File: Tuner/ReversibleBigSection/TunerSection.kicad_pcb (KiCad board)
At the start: 2 copper layers, 100 x 100 mm, 112 parts, among them J1 Conn_01x03, J10 Conn_01x02, J11 Conn_02x05_Odd_Even, J12 Conn_01x01, J13 Conn_01x01, J14 Conn_01x01, J15 Conn_01x01, J2 Conn_01x03, J3 Conn_01x03, J4 Conn_01x03, J5 Conn_01x03, J6 Conn_01x03, J7 Conn_01x03, J8 Conn_01x02, J9 Conn_01x02, P10 Conn_01x01, P11 Conn_01x01, P12 Conn_01x01, P2 Conn_01x01, P3 Conn_01x01, P4 Conn_01x01, P5 Conn_01x01, P6 Conn_01x01, P7 Conn_01x01, P8 Conn_01x01, P9 Conn_01x01, U1 MCP23008, U2 ULN2803A

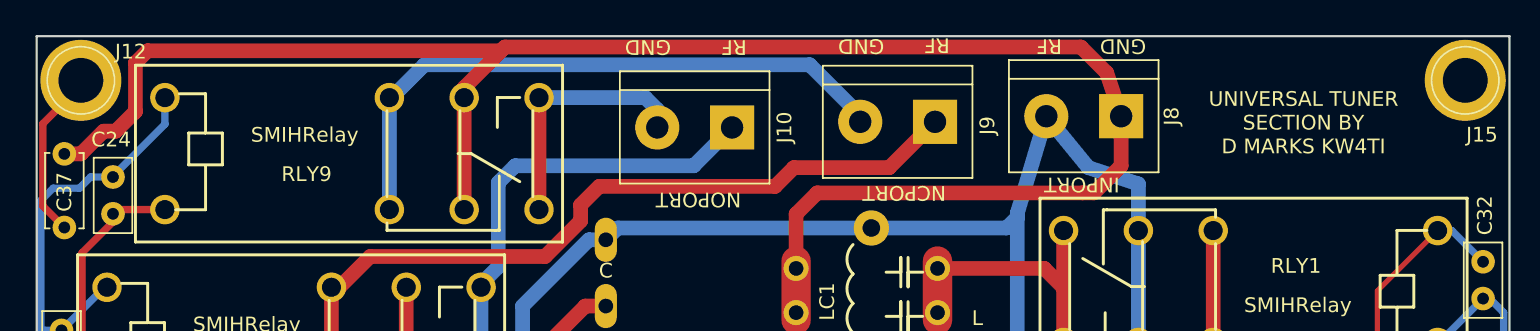
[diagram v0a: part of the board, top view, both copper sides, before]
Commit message: Added HK19F boards
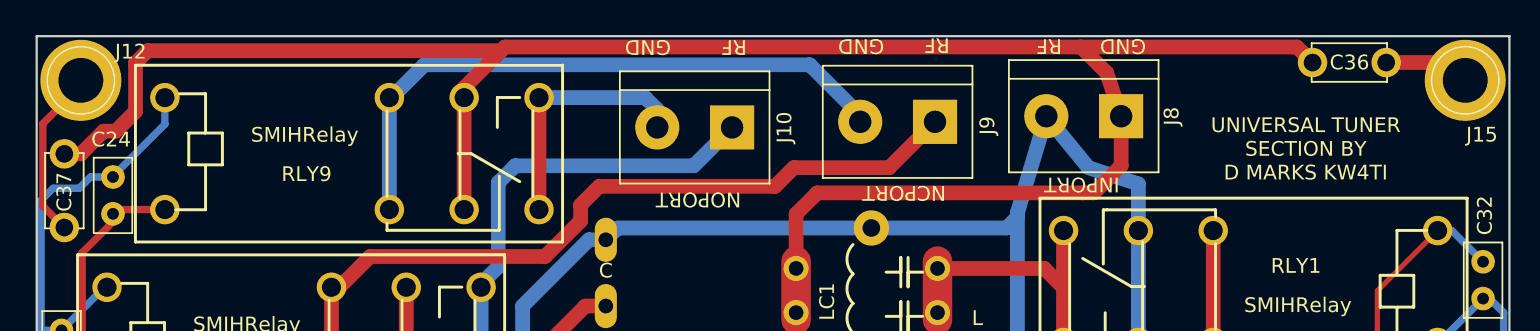
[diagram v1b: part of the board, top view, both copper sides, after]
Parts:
- added C36: 10 nF, Capacitors_THT:C_Disc_D5.0mm_W2.5mm_P5.00mm, F.Cu at (141.6, 51.8)
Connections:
- J15 pad 1: (no net) -> Net-(C36-Pad1)
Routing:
- net RFGND: track 185.3 -> 201.5 mm
- net Net-(C36-Pad1): track 0.00 -> 5.87 mm
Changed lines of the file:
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@@
 (kicad_pcb (version 4) (host pcbnew 4.0.7)
   (general
-    (links 280)
+    (links 282)
     (no_connects 0)
     (area 49.924999 49.924999 150.075001 150.075001)
     (thickness 1.6)
     (drawings 27)
-    (tracks 840)
+    (tracks 844)
     (zones 0)
-    (modules 112)
-    (nets 74)
+    (modules 113)
+    (nets 75)
   )
   (page A4)
@@
     (mod_text_size 1 1)
     (mod_text_width 0.15)
-    (pad_size 5.5 5.5)
-    (pad_drill 3.048)
+    (pad_size 2 2)
+    (pad_drill 1.2)
     (pad_to_mask_clearance 0.2)
     (aux_axis_origin 0 0)
@@
   (net 72 EXTPWR)
   (net 73 "Net-(C37-Pad1)")
+  (net 74 "Net-(C36-Pad1)")
   (net_class Default "This is the default net class."
     (clearance 0.2)
@@
     (add_net "Net-(C22-Pad1)")
     (add_net "Net-(C23-Pad2)")
+    (add_net "Net-(C36-Pad1)")
     (add_net "Net-(C37-Pad1)")
     (add_net "Net-(D1-Pad1)")
@@
     (fp_circle (center 0 0) (end 2.6 0) (layer F.CrtYd) (width 0.05))
     (fp_circle (center 0 0) (end 0 -2.286) (layer F.SilkS) (width 0.12))
-    (pad 1 thru_hole circle (at 0 0) (size 5.5 5.5) (drill 3.048) (layers *.Cu *.Mask))
+    (pad 1 thru_hole circle (at 0 0) (size 5.5 5.5) (drill 3.048) (layers *.Cu *.Mask)
+      (net 74 "Net-(C36-Pad1)"))
   )
   (module Capacitors_THT:C_Disc_D5.0mm_W2.5mm_P5.00mm (layer F.Cu)
@@
       (effects (font (size 1 1) (thickness 0.15)))
     )
-    (pad 1 thru_hole circle (at 0 0 90) (size 1.6 1.6) (drill 0.8) (layers *.Cu *.Mask)
+    (pad 1 thru_hole circle (at 0 0 90) (size 2 2) (drill 1.2) (layers *.Cu *.Mask)
       (net 73 "Net-(C37-Pad1)"))
-    (pad 2 thru_hole circle (at 5 0 90) (size 1.6 1.6) (drill 0.8) (layers *.Cu *.Mask)
+    (pad 2 thru_hole circle (at 5 0 90) (size 2 2) (drill 1.2) (layers *.Cu *.Mask)
       (net 1 RFGND))
     (model ${KISYS3DMOD}/Capacitors_THT.3dshapes/C_Disc_D5.0mm_W2.5mm_P5.00mm.wrl
@@
       (net 12 "Net-(J6-Pad2)"))
   )
+  (module Capacitors_THT:C_Disc_D5.0mm_W2.5mm_P5.00mm (layer F.Cu)
+    (at 141.6304 51.7906 180)
+    (descr "C, Disc series, Radial, pin pitch=5.00mm, , diameter*width=5*2.5mm^2, Capacitor, http://cdn-reichelt.de/documents/datenblatt/B300/DS_KERKO_TC.pdf")
+    (tags "C Disc series Radial pin pitch 5.00mm  diameter 5mm width 2.5mm Capacitor")
+    (fp_text reference C36 (at 2.4892 0 180) (layer F.SilkS)
+      (effects (font (size 1 1) (thickness 0.15)))
+    )
+    (fp_text value "10 nF" (at 2.5 2.56 180) (layer F.Fab)
+      (effects (font (size 1 1) (thickness 0.15)))
+    )
+    (fp_line (start 0 -1.25) (end 0 1.25) (layer F.Fab) (width 0.1))
+    (fp_line (start 0 1.25) (end 5 1.25) (layer F.Fab) (width 0.1))
+    (fp_line (start 5 1.25) (end 5 -1.25) (layer F.Fab) (width 0.1))
+    (fp_line (start 5 -1.25) (end 0 -1.25) (layer F.Fab) (width 0.1))
+    (fp_line (start -0.06 -1.31) (end 5.06 -1.31) (layer F.SilkS) (width 0.12))
+    (fp_line (start -0.06 1.31) (end 5.06 1.31) (layer F.SilkS) (width 0.12))
+    (fp_line (start -0.06 -1.31) (end -0.06 -0.996) (layer F.SilkS) (width 0.12))
+    (fp_line (start -0.06 0.996) (end -0.06 1.31) (layer F.SilkS) (width 0.12))
+    (fp_line (start 5.06 -1.31) (end 5.06 -0.996) (layer F.SilkS) (width 0.12))
+    (fp_line (start 5.06 0.996) (end 5.06 1.31) (layer F.SilkS) (width 0.12))
+    (fp_line (start -1.05 -1.6) (end -1.05 1.6) (layer F.CrtYd) (width 0.05))
+    (fp_line (start -1.05 1.6) (end 6.05 1.6) (layer F.CrtYd) (width 0.05))
+    (fp_line (start 6.05 1.6) (end 6.05 -1.6) (layer F.CrtYd) (width 0.05))
+    (fp_line (start 6.05 -1.6) (end -1.05 -1.6) (layer F.CrtYd) (width 0.05))
+    (fp_text user %R (at 2.5 0 180) (layer F.Fab)
+      (effects (font (size 1 1) (thickness 0.15)))
+    )
+    (pad 1 thru_hole circle (at 0 0 180) (size 2 2) (drill 1.2) (layers *.Cu *.Mask)
+      (net 74 "Net-(C36-Pad1)"))
+    (pad 2 thru_hole circle (at 5 0 180) (size 2 2) (drill 1.2) (layers *.Cu *.Mask)
+      (net 1 RFGND))
+    (model ${KISYS3DMOD}/Capacitors_THT.3dshapes/C_Disc_D5.0mm_W2.5mm_P5.00mm.wrl
+      (at (xyz 0 0 0))
+      (scale (xyz 1 1 1))
+      (rotate (xyz 0 0 0))
+    )
+  )
   (gr_text RF (at 97.3455 50.7365 180) (layer F.SilkS)
     (effects (font (size 1 1) (thickness 0.15)))
@@
   )
   (gr_line (start 150 50) (end 150 150) (angle 90) (layer Edge.Cuts) (width 0.15))
-  (gr_text "UNIVERSAL TUNER\nSECTION BY\nD MARKS KW4TI" (at 136.017 55.88) (layer F.SilkS)
+  (gr_text "UNIVERSAL TUNER\nSECTION BY\nD MARKS KW4TI" (at 136.1694 57.658) (layer F.SilkS)
     (effects (font (size 1 1) (thickness 0.15)))
   )
@@
   (segment (start 74.4616 110.0836) (end 74.772 110.394) (width 0.5) (layer B.Cu) (net 0))
   (segment (start 74.4616 110.0836) (end 74.772 110.394) (width 0.35) (layer B.Cu) (net 0))
+  (segment (start 120.904 50.7365) (end 135.5763 50.7365) (width 1) (layer F.Cu) (net 1))
+  (segment (start 135.5763 50.7365) (end 136.6304 51.7906) (width 1) (layer F.Cu) (net 1))
   (segment (start 121.031 60.6425) (end 121.793 60.6425) (width 1) (layer F.Cu) (net 1))
   (segment (start 123.6345 58.801) (end 123.6345 55.4355) (width 1) (layer F.Cu) (net 1) (status 20))
@@
   (segment (start 89.308 78.4495) (end 89.308 80.929) (width 1) (layer F.Cu) (net 22))
   (segment (start 80.1 79.8) (end 80.1 87.4) (width 1) (layer B.Cu) (net 22))
-  (segment (start 80.175 67.05) (end 80.175 66.8275) (width 1) (layer B.Cu) (net 23) (status C00000))
-  (segment (start 80.175 66.8275) (end 81.3435 65.659) (width 1) (layer B.Cu) (net 23) (status 400000))
-  (segment (start 94.615 58.801) (end 97.2185 56.1975) (width 1) (layer B.Cu) (net 23) (status 800000))
+  (segment (start 80.175 67.05) (end 80.175 66.8275) (width 1) (layer B.Cu) (net 23))
+  (segment (start 80.175 66.8275) (end 81.3435 65.659) (width 1) (layer B.Cu) (net 23))
+  (segment (start 94.615 58.801) (end 97.2185 56.1975) (width 1) (layer B.Cu) (net 23))
   (segment (start 82.4865 58.801) (end 94.615 58.801) (width 1) (layer B.Cu) (net 23))
   (segment (start 81.3435 59.944) (end 82.4865 58.801) (width 1) (layer B.Cu) (net 23))
@@
   (segment (start 76.327 51.943) (end 74.0945 54.1755) (width 1) (layer B.Cu) (net 39))
   (segment (start 74.0945 54.1755) (end 73.947 54.1755) (width 1) (layer B.Cu) (net 39))
-  (segment (start 84.107 54.1755) (end 84.107 61.7755) (width 1) (layer F.Cu) (net 40) (status C00000))
+  (segment (start 84.107 54.1755) (end 84.107 61.7755) (width 1) (layer F.Cu) (net 40))
   (segment (start 92.1385 56.1975) (end 92.1385 54.991) (width 1) (layer B.Cu) (net 40))
   (segment (start 92.1385 54.991) (end 91.323 54.1755) (width 1) (layer B.Cu) (net 40))
@@
   (segment (start 50.419 55.9435) (end 50.419 61.5315) (width 0.5) (layer F.Cu) (net 73))
   (segment (start 52.13604 53.86396) (end 53 53) (width 1) (layer F.Cu) (net 73) (status 30))
+  (segment (start 141.6304 51.7906) (end 145.7906 51.7906) (width 1) (layer F.Cu) (net 74))
+  (segment (start 145.7906 51.7906) (end 147 53) (width 1) (layer F.Cu) (net 74))
   (zone (net 25) (net_name GND) (layer F.Cu) (hatch edge 0.508)
     (connect_pads (clearance 0.5))

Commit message: JLCPCB Nov 1 2018
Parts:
- removed C36, C37: 10 nF, Capacitors_THT:C_Disc_D5.0mm_W2.5mm_P5.00mm
- added J16: Conn_01x01, tuner:SOLDERJUMPER, F.Cu at (74.5, 51.0)
- added J17: Conn_01x01, tuner:SOLDERJUMPER, F.Cu at (129.1, 52.9)
- added J18: Conn_01x01, tuner:SOLDERJUMPER, F.Cu at (141.8, 51.8)
- added J19: Conn_01x01, tuner:SOLDERJUMPER, F.Cu at (138.6, 51.8)
- added J20: Conn_01x01, tuner:SOLDERJUMPER, F.Cu at (60.0, 50.9)
- added J21: Conn_01x01, tuner:SOLDERJUMPER, F.Cu at (64.8, 50.9)
- added J22: Conn_01x01, tuner:SOLDERJUMPER, F.Cu at (88.5, 56.7)
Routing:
- net RFGND: track 201.5 -> 156.1 mm
- net Net-(J16-Pad1): track 42.4 -> 45.9 mm
- net Net-(J15-Pad1): track 5.87 -> 9.39 mm
- net Net-(J10-Pad2): track 17.2 -> 19.9 mm

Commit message: First code commit
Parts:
- moved RLY9 0.64 mm to (68.7, 57.3)
- moved RLY8 0.44 mm to (64.8, 70.4)
- moved RLY7 0.20 mm to (64.6, 83.4)
- moved RLY6 0.13 mm to (64.6, 96.5)
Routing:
- net RLYPWR: track 358.8 -> 359.8 mm

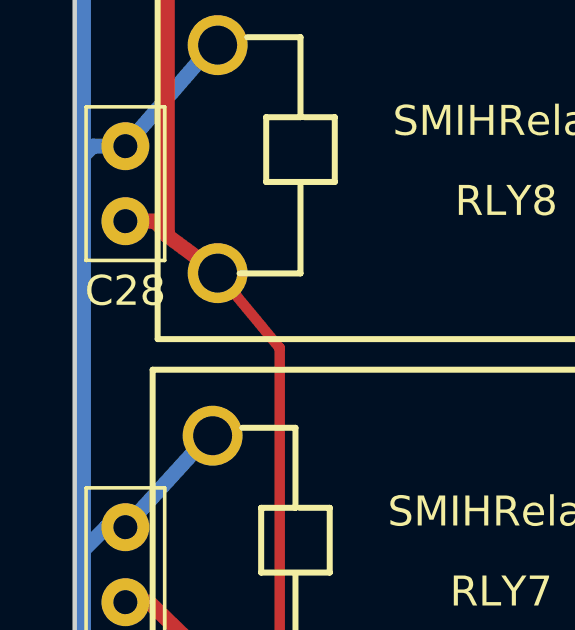
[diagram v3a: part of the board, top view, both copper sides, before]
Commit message: Removed 1k resistors, did some more rearranging on TandemMatch
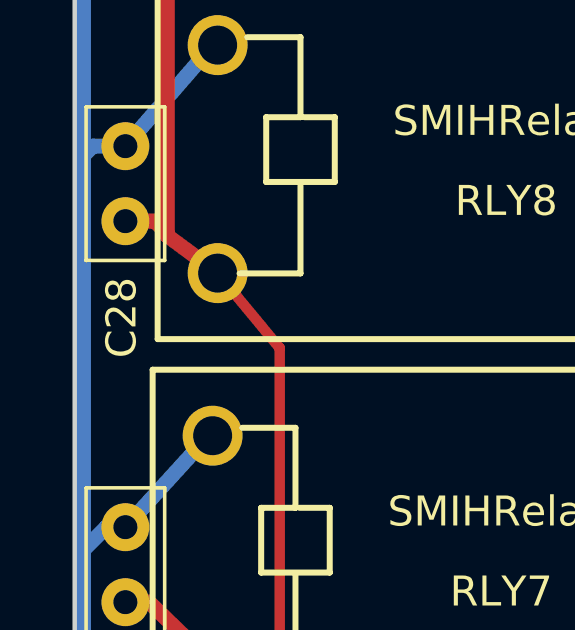
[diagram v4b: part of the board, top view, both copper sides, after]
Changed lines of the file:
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@@
     (links 285)
     (no_connects 0)
-    (area 44.281218 45.69208 151.844 153.921938)
+    (area 49.924999 49.924999 150.075001 150.075001)
     (thickness 1.6)
     (drawings 27)
@@
     (descr "C, Disc series, Radial, pin pitch=2.50mm, , diameter*width=5*2.5mm^2, Capacitor, http://cdn-reichelt.de/documents/datenblatt/B300/DS_KERKO_TC.pdf")
     (tags "C Disc series Radial pin pitch 2.50mm  diameter 5mm width 2.5mm Capacitor")
-    (fp_text reference C28 (at 4.826 0 360) (layer F.SilkS)
+    (fp_text reference C28 (at 5.715 0.127 450) (layer F.SilkS)
       (effects (font (size 1 1) (thickness 0.15)))
     )

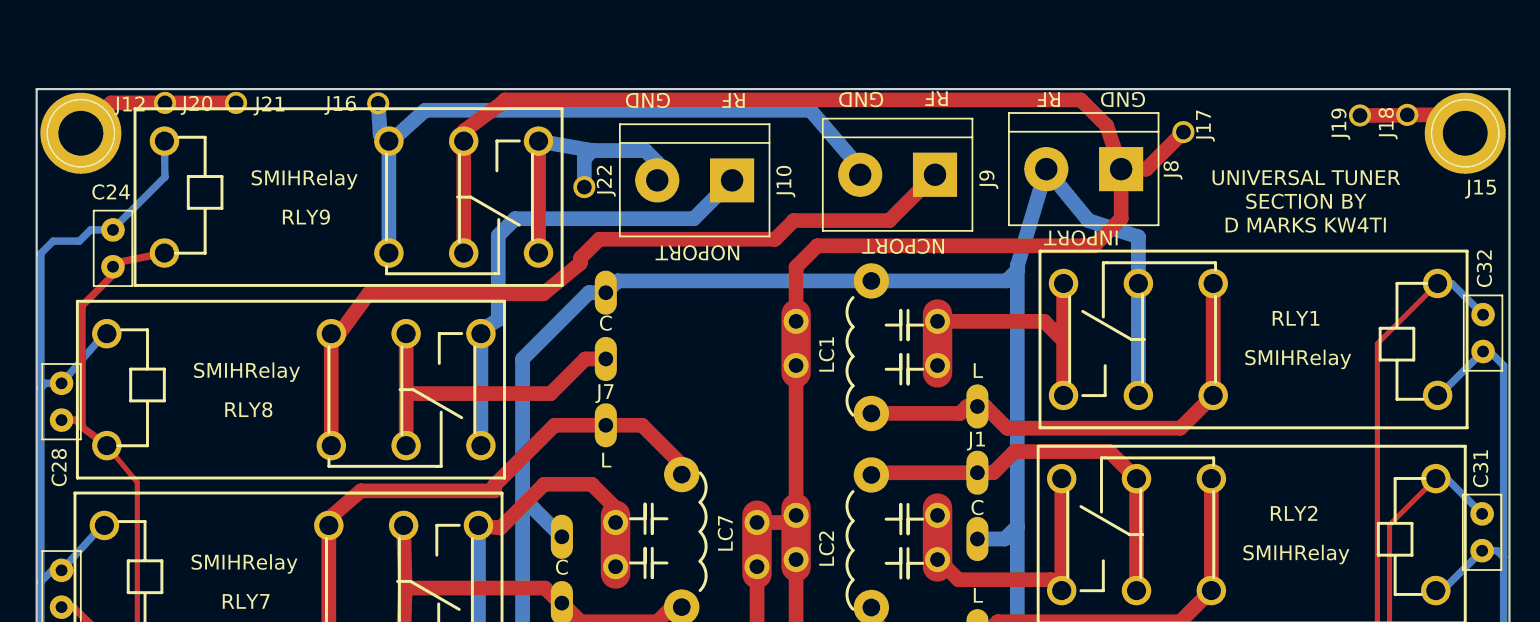
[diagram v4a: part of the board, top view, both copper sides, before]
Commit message: Modified connectors on Reversible boards
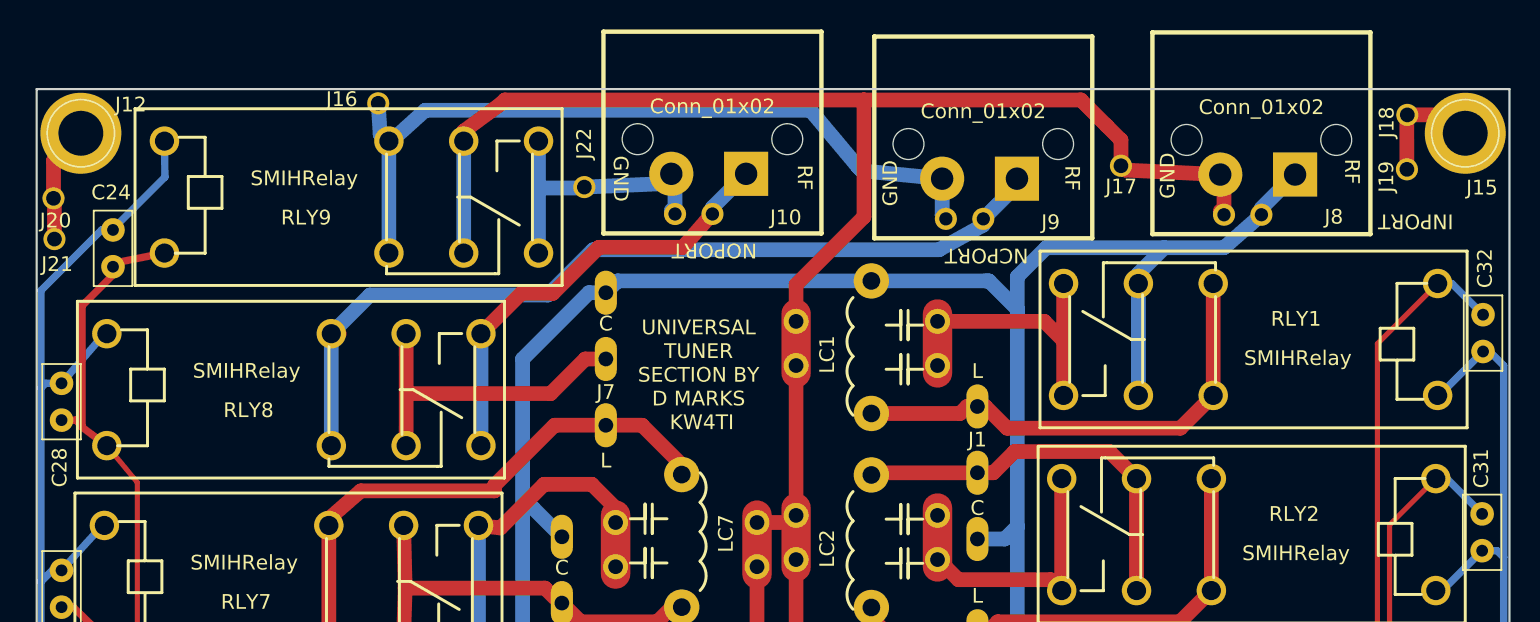
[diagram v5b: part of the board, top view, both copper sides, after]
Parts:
- J10, J8, J9: footprint Connectors_Terminal_Blocks:TerminalBlock_bornier-2_P5.08mm -> tuner:bnc_90_1-1337543-0_pad_combo
- moved J21 15.4 mm to (52.5, 60.2)
- moved J8 13.3 mm to (133.2, 46.2)
- moved J10 10.2 mm to (95.9, 46.1)
- moved J20 9.96 mm to (52.4, 57.4)
- moved J9 9.94 mm to (114.3, 46.4)
- moved J19 4.85 mm to (141.8, 55.4)
- moved J17 4.82 mm to (124.9, 55.2)
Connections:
- J8 pad 1: RFGND -> RFPORT1
- J8 pad 2: RFPORT1 -> RFGND
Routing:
- net RFGND: track 155.7 -> 147.0 mm
- net Net-(J16-Pad1): track 45.5 -> 53.6 mm
- net RFPORT1: track 161.1 -> 168.9 mm
- net Net-(J9-Pad1): track 53.4 -> 59.3 mm
- net Net-(J12-Pad1): track 13.0 -> 9.57 mm
- net Net-(J10-Pad1): track 32.3 -> 30.7 mm
- net RLYPWR: track 359.8 -> 358.3 mm

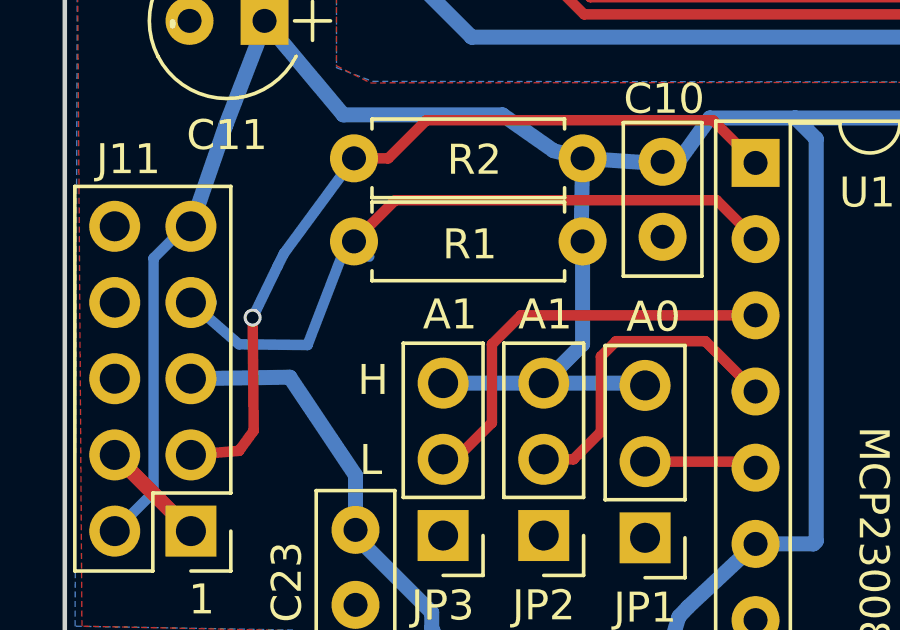
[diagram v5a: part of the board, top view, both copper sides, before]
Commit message: Symmetrized QuadCoupler Layout
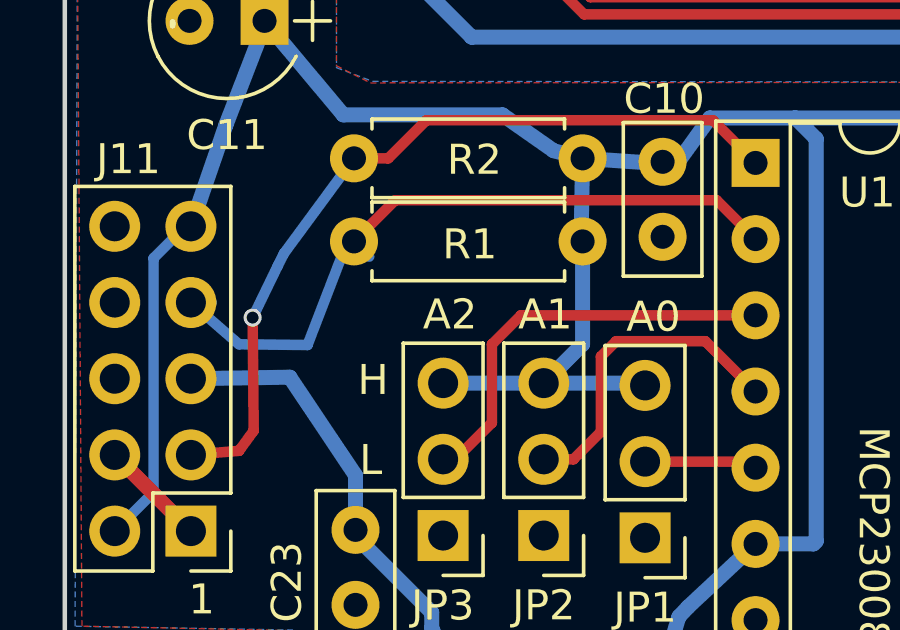
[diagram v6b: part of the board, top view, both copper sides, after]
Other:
- board text added: "A2"
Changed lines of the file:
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@@
     (links 291)
     (no_connects 0)
-    (area 49.924999 49.924999 150.075001 150.075001)
+    (area 44.281218 45.651 151.844 153.921938)
     (thickness 1.6)
     (drawings 27)
@@
   )
   (setup
-    (last_trace_width 1)
+    (last_trace_width 0.25)
     (user_trace_width 0.35)
     (user_trace_width 0.5)
@@
     (effects (font (size 1 1) (thickness 0.15)))
   )
-  (gr_text A1 (at 62.8396 132.8166) (layer F.SilkS)
+  (gr_text A2 (at 62.8396 132.8166) (layer F.SilkS)
     (effects (font (size 1 1) (thickness 0.15)))
   )

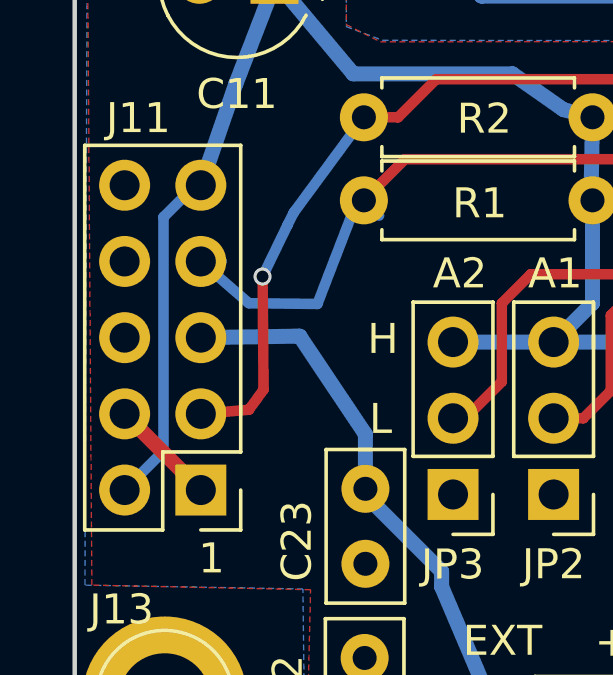
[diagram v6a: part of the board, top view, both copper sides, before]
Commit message: Changed I2C cable pinoutgit add Tunergit add Tuner Also added ICOM rig support
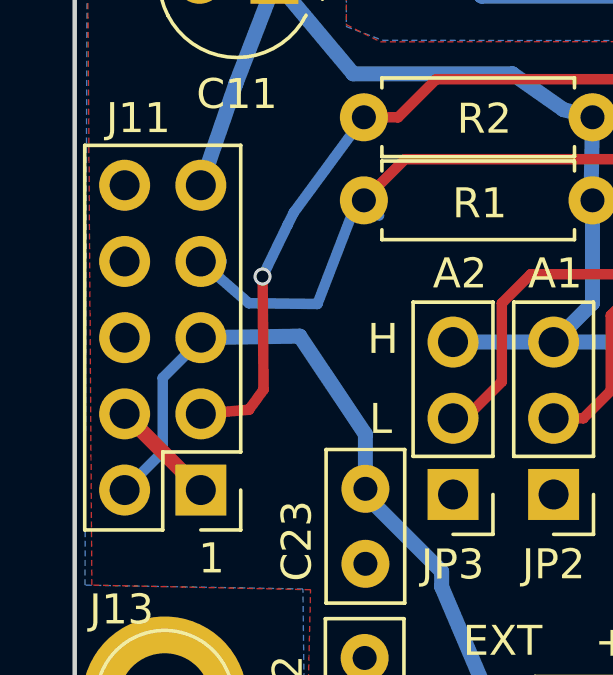
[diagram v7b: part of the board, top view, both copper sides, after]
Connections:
- J11 pad 2: +5V -> Net-(C23-Pad2)
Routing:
- net +5V: track 89.8 -> 78.2 mm
- net Net-(C23-Pad2): track 18.1 -> 24.2 mm

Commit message: JLCPCB order 2019-03-25
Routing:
- net GND: track 68.0 -> 237.2 mm, vias 0 -> 29
